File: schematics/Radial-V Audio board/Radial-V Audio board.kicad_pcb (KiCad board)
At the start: 2 copper layers, 100 x 45 mm, 15 parts, among them J1 Audio IN left, J2 Audio IN right, J3 Slot PreAmplifier, J4 Power Supply, J5 Volume, J6 Alim Ampli, J7 To Amplifier, J8 From Amplifier, J9 Audio OUT (mono)

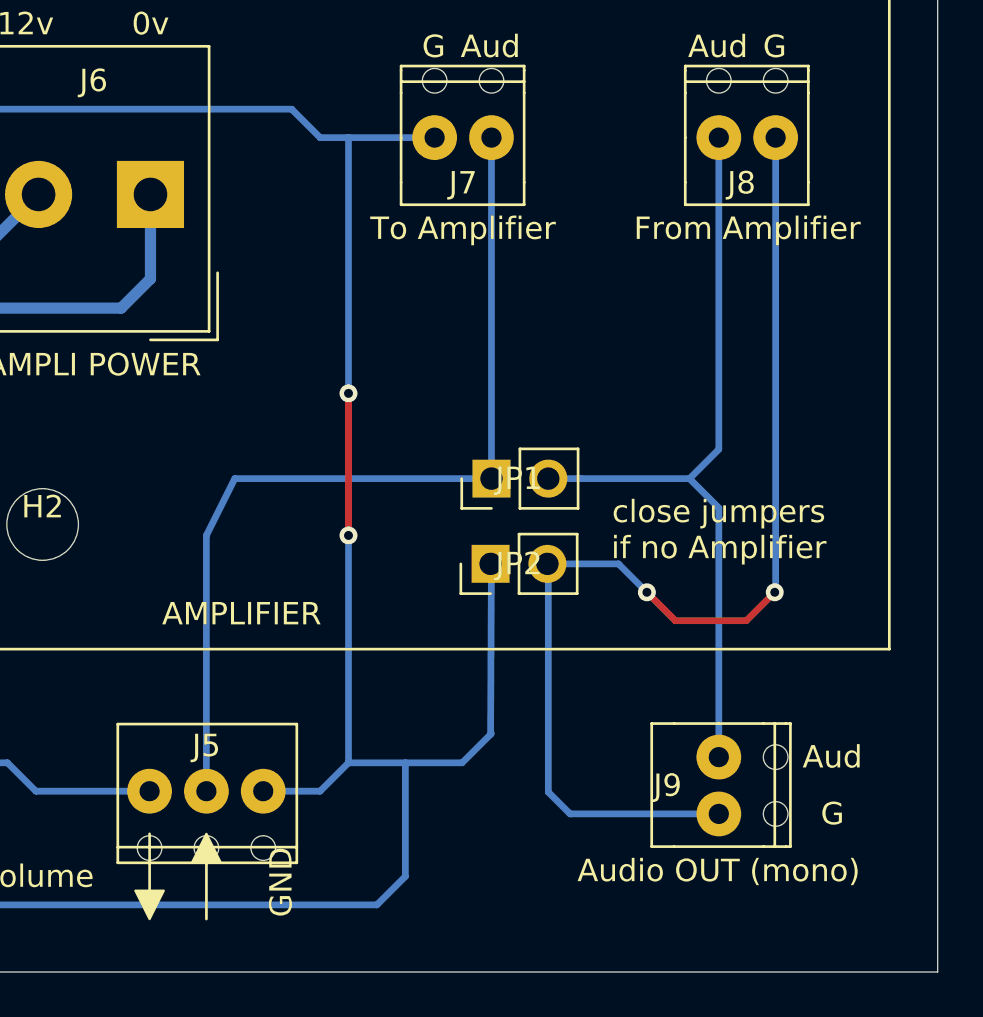
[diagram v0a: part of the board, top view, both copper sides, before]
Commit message: wire fix
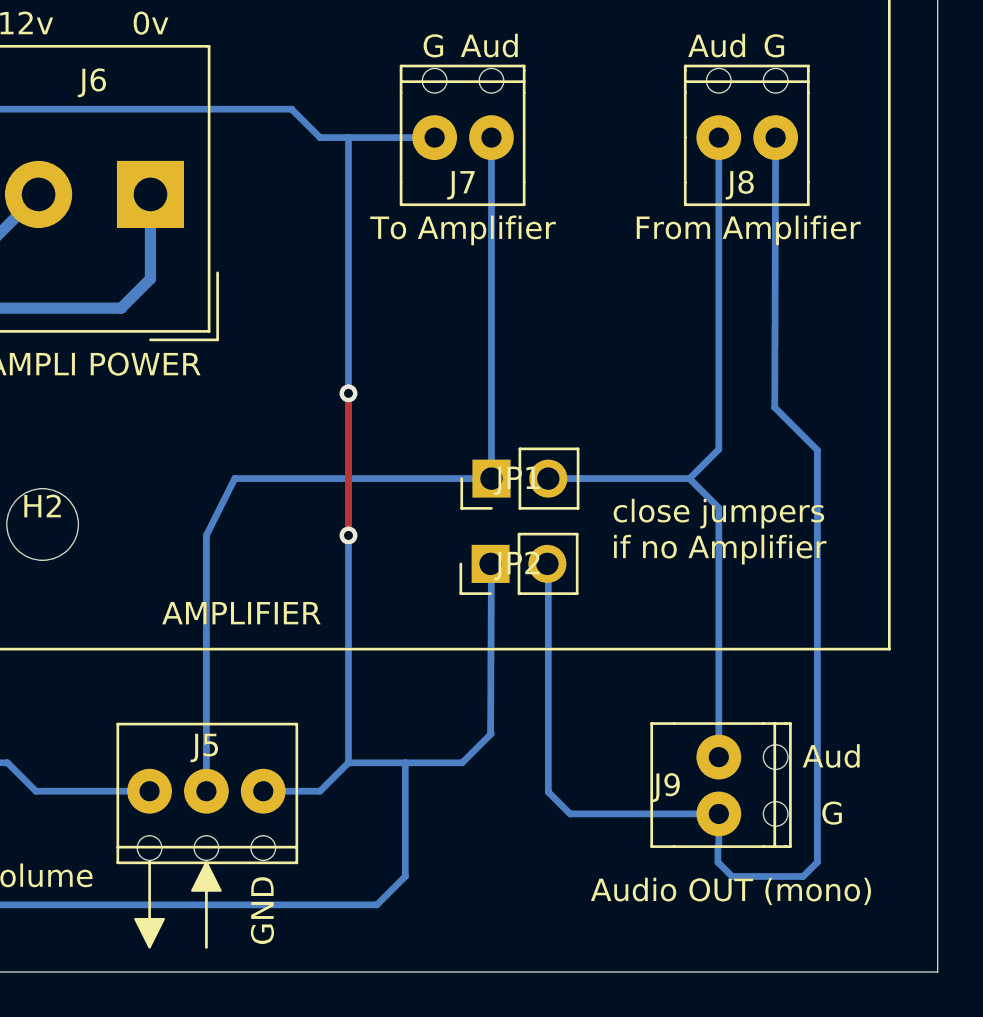
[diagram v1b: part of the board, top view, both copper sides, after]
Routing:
- net /GND_OUT: track 50.6 -> 58.8 mm, vias 2 -> 0
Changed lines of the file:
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@@
       (effects (font (size 1 1) (thickness 0.15)))
     )
-    (fp_text user %V (at 5.08 0 180) (layer F.SilkS)
+    (fp_text user %V (at 5.969 -0.595 180) (layer F.SilkS)
       (effects (font (size 1 1) (thickness 0.15)))
     )
@@
   (gr_line (start 80 85) (end 180 85) (layer Edge.Cuts) (width 0.05))
   (gr_line (start 80 130) (end 80 85) (layer Edge.Cuts) (width 0.05))
-  (gr_line (start 147.32 125.095) (end 147.32 127.635) (layer F.SilkS) (width 0.12))
-  (gr_line (start 144.78 123.825) (end 144.78 126.365) (layer F.SilkS) (width 0.12))
-  (gr_poly (pts (xy 147.955 125.095) (xy 146.685 125.095) (xy 147.32 123.825)) (layer F.SilkS) (width 0.1))
-  (gr_poly (pts (xy 144.78 127.635) (xy 144.145 126.365) (xy 145.415 126.365)) (layer F.SilkS) (width 0.1))
+  (gr_line (start 147.32 126.365) (end 147.32 128.905) (layer F.SilkS) (width 0.12))
+  (gr_line (start 144.78 125.095) (end 144.78 127.635) (layer F.SilkS) (width 0.12))
+  (gr_poly (pts (xy 147.955 126.365) (xy 146.685 126.365) (xy 147.32 125.095)) (layer F.SilkS) (width 0.1))
+  (gr_poly (pts (xy 144.78 128.905) (xy 144.145 127.635) (xy 145.415 127.635)) (layer F.SilkS) (width 0.1))
   (gr_line (start 180 130) (end 80 130) (layer Edge.Cuts) (width 0.05))
   (gr_line (start 180 85) (end 180 130) (layer Edge.Cuts) (width 0.05))
@@
     (effects (font (size 1 1) (thickness 0.15)))
   )
-  (gr_text GND (at 150.662 125.984 90) (layer F.SilkS)
+  (gr_text GND (at 149.86 127.254 90) (layer F.SilkS)
     (effects (font (size 1 1) (thickness 0.15)))
   )
@@
   (segment (start 163.576 122.936) (end 170.22 122.936) (width 0.3) (layer B.Cu) (net 13))
   (segment (start 162.6 121.96) (end 163.576 122.936) (width 0.3) (layer B.Cu) (net 13))
-  (via (at 172.72 113.03) (size 0.8) (drill 0.4) (layers F.Cu B.Cu) (net 13))
-  (segment (start 172.76 92.71) (end 172.76 112.99) (width 0.3) (layer B.Cu) (net 13))
-  (segment (start 172.76 112.99) (end 172.72 113.03) (width 0.3) (layer B.Cu) (net 13))
-  (segment (start 172.72 113.03) (end 171.45 114.3) (width 0.3) (layer F.Cu) (net 13))
-  (via (at 167.005 113.03) (size 0.8) (drill 0.4) (layers F.Cu B.Cu) (net 13))
-  (segment (start 171.45 114.3) (end 168.275 114.3) (width 0.3) (layer F.Cu) (net 13))
-  (segment (start 168.275 114.3) (end 167.005 113.03) (width 0.3) (layer F.Cu) (net 13))
-  (segment (start 165.735 111.76) (end 162.56 111.76) (width 0.3) (layer B.Cu) (net 13))
-  (segment (start 167.005 113.03) (end 165.735 111.76) (width 0.3) (layer B.Cu) (net 13))
+  (segment (start 172.72 104.775) (end 172.76 92.71) (width 0.3) (layer B.Cu) (net 13))
+  (segment (start 174.625 106.68) (end 172.72 104.775) (width 0.3) (layer B.Cu) (net 13))
+  (segment (start 174.625 125.095) (end 174.625 106.68) (width 0.3) (layer B.Cu) (net 13))
+  (segment (start 170.22 124.350213) (end 170.18 124.390213) (width 0.3) (layer B.Cu) (net 13))
+  (segment (start 170.18 125.095) (end 170.815 125.73) (width 0.3) (layer B.Cu) (net 13))
+  (segment (start 173.99 125.73) (end 174.625 125.095) (width 0.3) (layer B.Cu) (net 13))
+  (segment (start 170.22 122.936) (end 170.22 124.350213) (width 0.3) (layer B.Cu) (net 13))
+  (segment (start 170.18 124.390213) (end 170.18 125.095) (width 0.3) (layer B.Cu) (net 13))
+  (segment (start 170.815 125.73) (end 173.99 125.73) (width 0.3) (layer B.Cu) (net 13))
 )

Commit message: Update Audio Board
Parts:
- J3: footprint Connector_JST:JST_VH_B10P-VH-B_1x10_P3.96mm_Vertical -> MesModules:Edge_Connector_10P_1x10_P3.96mm_Vertical
